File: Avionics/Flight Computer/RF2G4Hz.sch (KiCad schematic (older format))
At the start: 39 parts, among them J5 734120110, U3 CC2650F128RGZR, U4 CC2592RGVR, Y5 XRCGB24M000F2P00R0

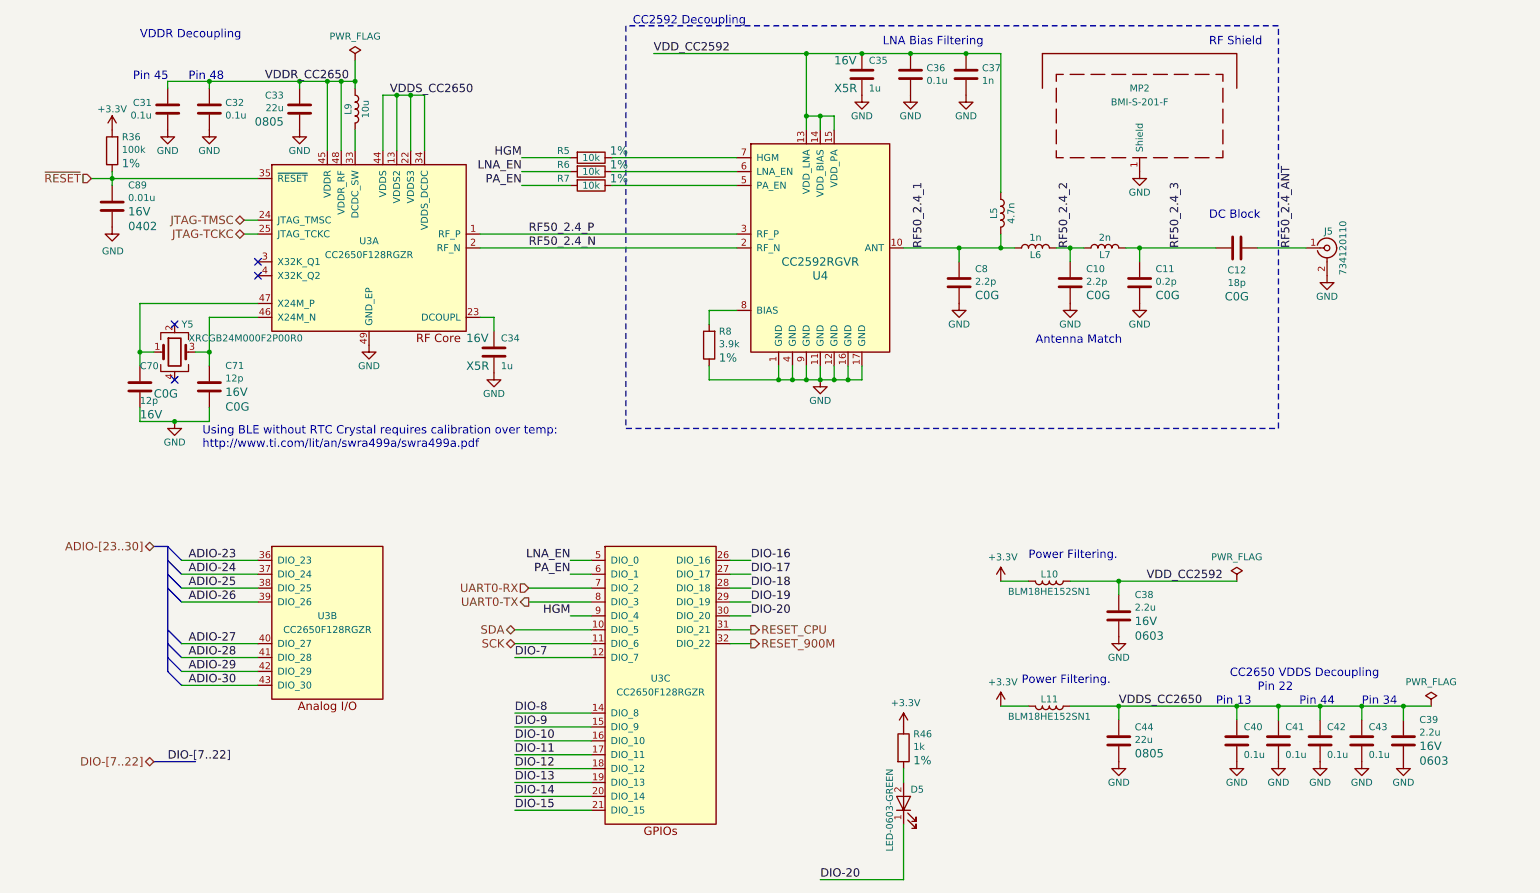
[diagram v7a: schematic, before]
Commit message: Built outputs and added manufacturing part numbers to make BOM search easier.
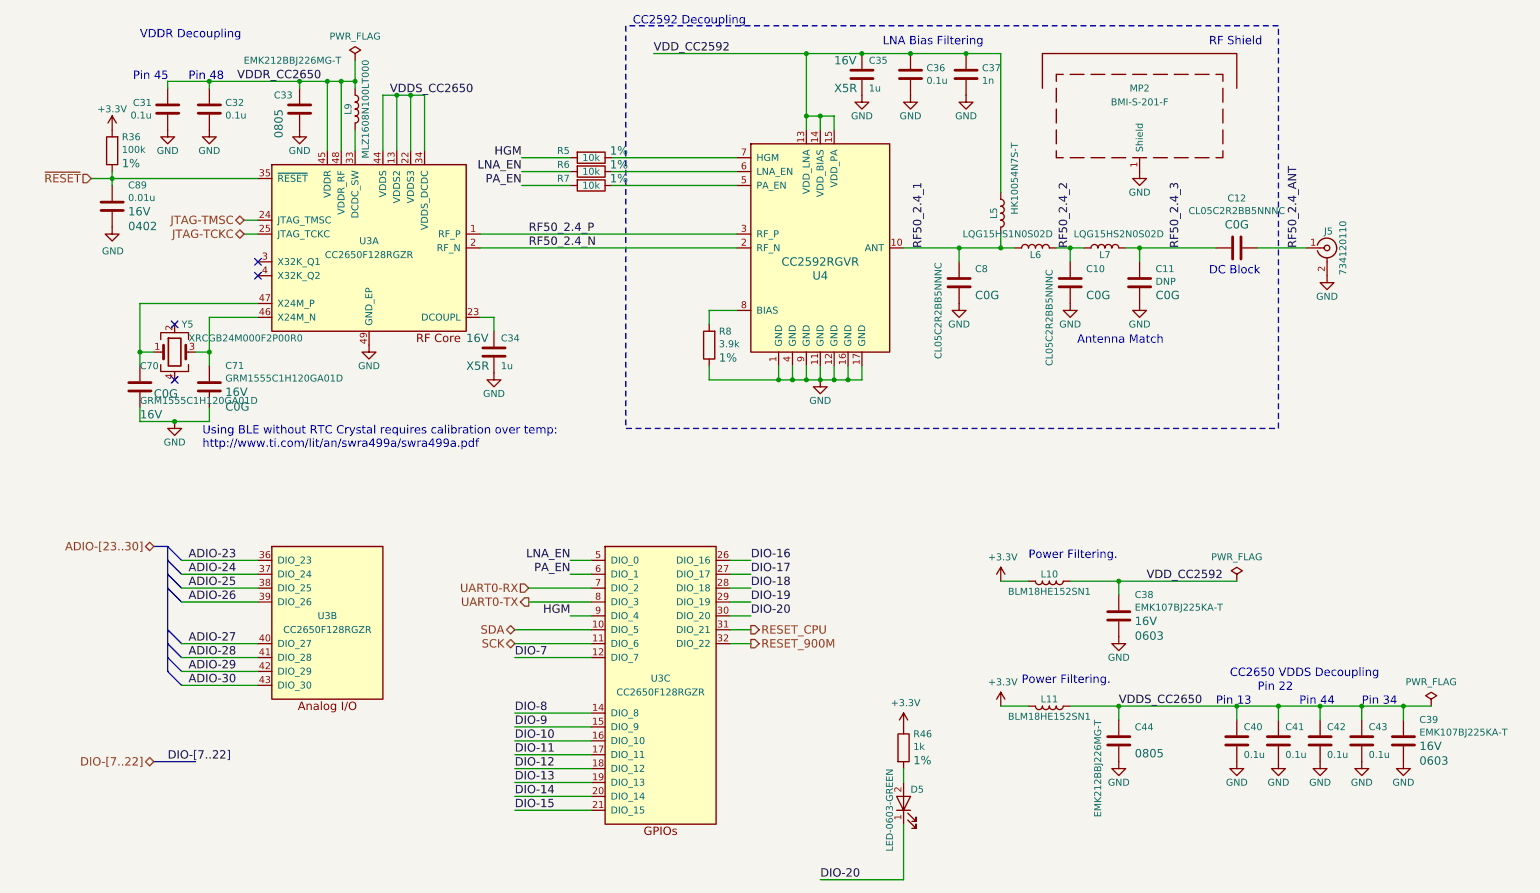
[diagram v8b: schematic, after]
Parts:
- C10, C8: value 2.2p -> CL05C2R2BB5NNNC
- C11: value 0.2p -> DNP
- C12: value 18p -> CL05C2R2BB5NNNC
- C33, C44: value 22u -> EMK212BBJ226MG-T
- C38, C39: value 2.2u -> EMK107BJ225KA-T
- C70, C71: value 12p -> GRM1555C1H120GA01D
- L5: value 4.7n -> HK10054N7S-T
- L6: value 1n -> LQG15HS1N0S02D
- L7: value 2n -> LQG15HS2N0S02D
- L9: value 10u -> MLZ1608N100LT000
